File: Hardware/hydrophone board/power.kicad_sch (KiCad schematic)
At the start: 17 parts, among them J203 Screw_Terminal_01x02, U5 LT1963AxST-3.3

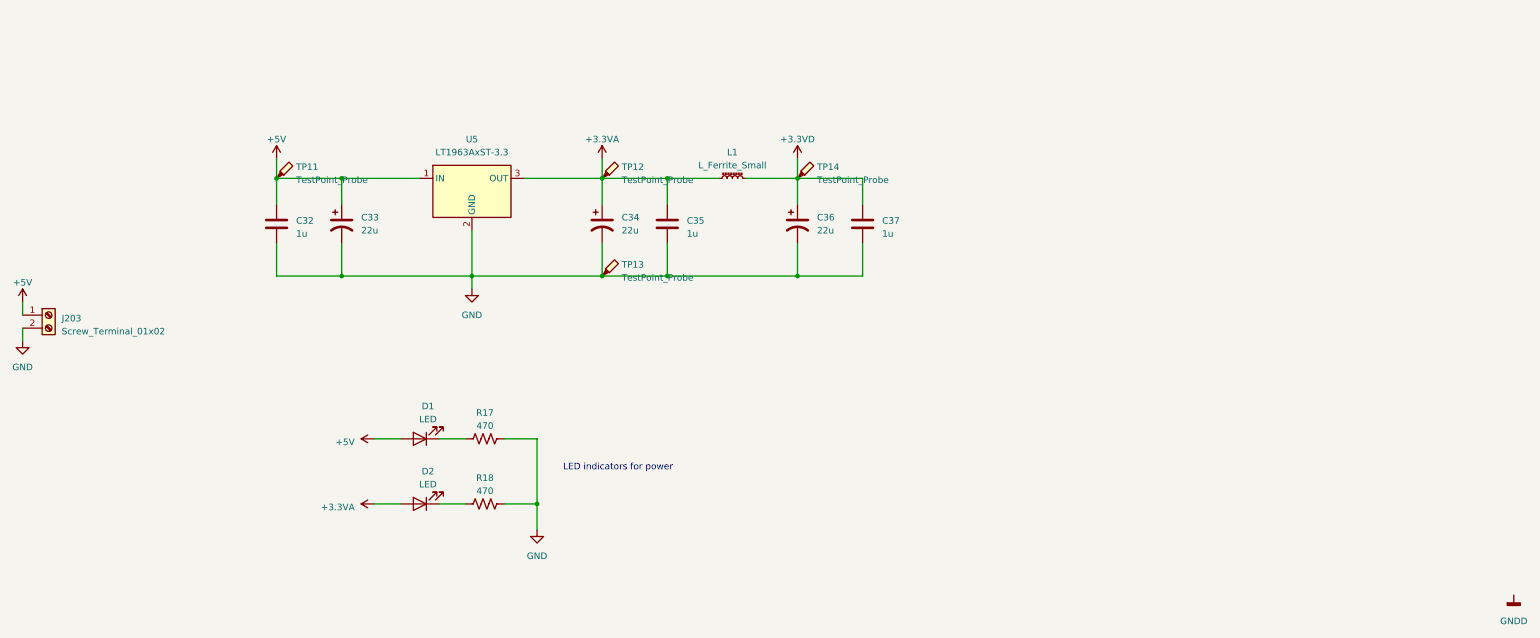
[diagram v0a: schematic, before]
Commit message: i2c pull ups
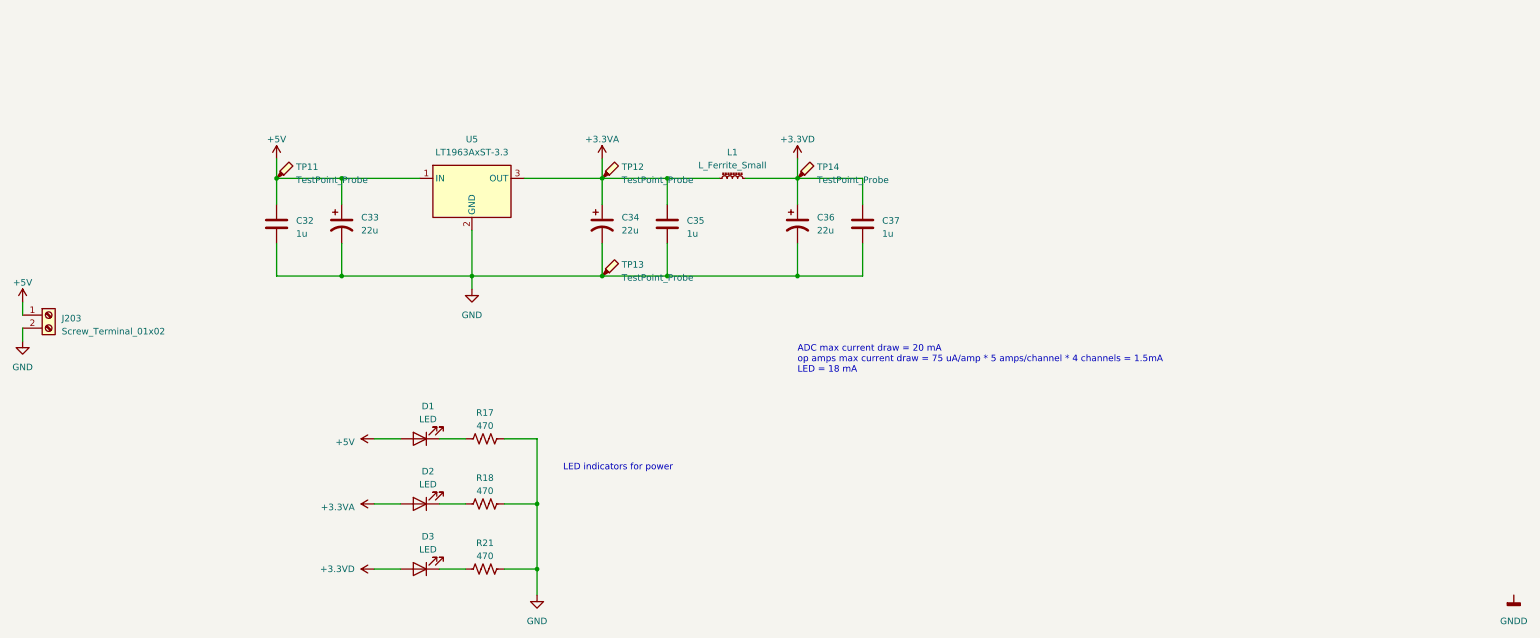
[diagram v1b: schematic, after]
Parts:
- added D3: LED, symbol Device:LED
- added R21: 470, symbol Device:R_US
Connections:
- net +3.3VD: now also D3.2 (A)
- net GND: now also R21.2
- new net: D3.1 (K), R21.1
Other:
- note added: "ADC max current draw = 20 mA op amps max current draw = 75 uA/amp * 5 amps/channel * 4 channels = 1.5mA LED = 18 mA"
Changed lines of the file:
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@@
   (junction (at 165.1 95.25) (diameter 0) (color 0 0 0 0)
   )
+  (junction (at 139.7 152.4) (diameter 0) (color 0 0 0 0)
+  )
   (junction (at 101.6 76.2) (diameter 0) (color 0 0 0 0)
   )
@@
     (stroke (width 0) (type default))
   )
-  (wire (pts (xy 139.7 139.7) (xy 139.7 144.78))
+  (wire (pts (xy 139.7 139.7) (xy 139.7 152.4))
     (stroke (width 0) (type default))
   )
@@
     (stroke (width 0) (type default))
   )
+  (wire (pts (xy 107.95 152.4) (xy 113.03 152.4))
+    (stroke (width 0) (type default))
+  )
   (wire (pts (xy 180.34 76.2) (xy 190.5 76.2))
     (stroke (width 0) (type default))
@@
     (stroke (width 0) (type default))
   )
+  (wire (pts (xy 120.65 152.4) (xy 125.73 152.4))
+    (stroke (width 0) (type default))
+  )
   (wire (pts (xy 107.95 127) (xy 113.03 127))
     (stroke (width 0) (type default))
   )
+  (wire (pts (xy 133.35 152.4) (xy 139.7 152.4))
+    (stroke (width 0) (type default))
+  )
   (wire (pts (xy 101.6 76.2) (xy 101.6 81.28))
     (stroke (width 0) (type default))
@@
     (stroke (width 0) (type default))
   )
+  (wire (pts (xy 139.7 152.4) (xy 139.7 157.48))
+    (stroke (width 0) (type default))
+  )
   (wire (pts (xy 165.1 76.2) (xy 165.1 81.28))
     (stroke (width 0) (type default))
+  )
+  (text "ADC max current draw = 20 mA\nop amps max current draw = 75 uA/amp * 5 amps/channel * 4 channels = 1.5mA\nLED = 18 mA"
+    (at 190.5 114.3 0)
+    (effects (font (size 1.27 1.27)) (justify left bottom))
   )
   (text "LED indicators for power" (at 144.78 133.35 0)
@@
     )
   )
+  (symbol (lib_id "power:+3.3V") (at 107.95 152.4 90) (unit 1)
+    (in_bom yes) (on_board yes) (dnp no) (fields_autoplaced)
+    (property "Reference" "#PWR?" (at 111.76 152.4 0)
+      (effects (font (size 1.27 1.27)) hide)
+    )
+    (property "Value" "+3.3VD" (at 104.14 152.4 90)
+      (effects (font (size 1.27 1.27)) (justify left))
+    )
+    (property "Footprint" "" (at 107.95 152.4 0)
+      (effects (font (size 1.27 1.27)) hide)
+    )
+    (property "Datasheet" "" (at 107.95 152.4 0)
+      (effects (font (size 1.27 1.27)) hide)
+    )
+    (pin "1")
+    (instances
+      (project "hydrophone board"
+        (path "/4356d3a6-6a00-447d-897e-473f60221539/c9760799-658d-4181-af96-8731ebbcaea9"
+          (reference "#PWR?") (unit 1)
+        )
+        (path "/4356d3a6-6a00-447d-897e-473f60221539/cf9d259f-9643-49eb-8aca-1ca8b75f4d64"
+          (reference "#PWR036") (unit 1)
+        )
+      )
+    )
+  )
   (symbol (lib_id "power:GND") (at 39.37 107.95 0) (unit 1)
     (in_bom yes) (on_board yes) (dnp no) (fields_autoplaced)
@@
     )
   )
+  (symbol (lib_id "Device:R_US") (at 129.54 152.4 90) (unit 1)
+    (in_bom yes) (on_board yes) (dnp no) (fields_autoplaced)
+    (property "Reference" "R21" (at 129.54 147.32 90)
+      (effects (font (size 1.27 1.27)))
+    )
+    (property "Value" "470" (at 129.54 149.86 90)
+      (effects (font (size 1.27 1.27)))
+    )
+    (property "Footprint" "" (at 129.794 151.384 90)
+      (effects (font (size 1.27 1.27)) hide)
+    )
+    (property "Datasheet" "~" (at 129.54 152.4 0)
+      (effects (font (size 1.27 1.27)) hide)
+    )
+    (pin "1")
+    (pin "2")
+    (instances
+      (project "hydrophone board"
+        (path "/4356d3a6-6a00-447d-897e-473f60221539/cf9d259f-9643-49eb-8aca-1ca8b75f4d64"
+          (reference "R21") (unit 1)
+        )
+      )
+    )
+  )
   (symbol (lib_id "Device:C_Polarized_US") (at 152.4 85.09 0) (unit 1)
     (in_bom yes) (on_board yes) (dnp no) (fields_autoplaced)
@@
         (path "/4356d3a6-6a00-447d-897e-473f60221539/cf9d259f-9643-49eb-8aca-1ca8b75f4d64"
           (reference "C34") (unit 1)
+        )
+      )
+    )
+  )
+  (symbol (lib_id "power:GND") (at 139.7 157.48 0) (unit 1)
+    (in_bom yes) (on_board yes) (dnp no) (fields_autoplaced)
+    (property "Reference" "#PWR0205" (at 139.7 163.83 0)
+      (effects (font (size 1.27 1.27)) hide)
+    )
+    (property "Value" "GND" (at 139.7 162.56 0)
+      (effects (font (size 1.27 1.27)))
+    )
+    (property "Footprint" "" (at 139.7 157.48 0)
+      (effects (font (size 1.27 1.27)) hide)
+    )
+    (property "Datasheet" "" (at 139.7 157.48 0)
+      (effects (font (size 1.27 1.27)) hide)
+    )
+    (pin "1")
+    (instances
+      (project "hydrophone board"
+        (path "/4356d3a6-6a00-447d-897e-473f60221539/1cfbaf71-7039-4355-8fc7-d8c77f0e8058"
+          (reference "#PWR0205") (unit 1)
+        )
+        (path "/4356d3a6-6a00-447d-897e-473f60221539/cf9d259f-9643-49eb-8aca-1ca8b75f4d64"
+          (reference "#PWR045") (unit 1)
         )
       )
@@
     )
   )
-  (symbol (lib_id "power:GND") (at 139.7 144.78 0) (unit 1)
-    (in_bom yes) (on_board yes) (dnp no) (fields_autoplaced)
-    (property "Reference" "#PWR0205" (at 139.7 151.13 0)
-      (effects (font (size 1.27 1.27)) hide)
-    )
-    (property "Value" "GND" (at 139.7 149.86 0)
-      (effects (font (size 1.27 1.27)))
-    )
-    (property "Footprint" "" (at 139.7 144.78 0)
-      (effects (font (size 1.27 1.27)) hide)
-    )
-    (property "Datasheet" "" (at 139.7 144.78 0)
-      (effects (font (size 1.27 1.27)) hide)
-    )
-    (pin "1")
-    (instances
-      (project "hydrophone board"
-        (path "/4356d3a6-6a00-447d-897e-473f60221539/1cfbaf71-7039-4355-8fc7-d8c77f0e8058"
-          (reference "#PWR0205") (unit 1)
-        )
-        (path "/4356d3a6-6a00-447d-897e-473f60221539/cf9d259f-9643-49eb-8aca-1ca8b75f4d64"
-          (reference "#PWR036") (unit 1)
-        )
-      )
-    )
-  )
   (symbol (lib_id "Device:LED") (at 116.84 127 180) (unit 1)
     (in_bom yes) (on_board yes) (dnp no) (fields_autoplaced)
@@
         )
       )
+    )
+  )
+  (symbol (lib_id "Device:LED") (at 116.84 152.4 180) (unit 1)
+    (in_bom yes) (on_board yes) (dnp no) (fields_autoplaced)
+    (property "Reference" "D3" (at 118.4275 146.05 0)
+      (effects (font (size 1.27 1.27)))
+    )
+    (property "Value" "LED" (at 118.4275 148.59 0)
+      (effects (font (size 1.27 1.27)))
+    )
+    (property "Footprint" "" (at 116.84 152.4 0)
+      (effects (font (size 1.27 1.27)) hide)
+    )
+    (property "Datasheet" "~" (at 116.84 152.4 0)
+      (effects (font (size 1.27 1.27)) hide)
+    )
+    (pin "1")
+    (pin "2")
+    (instances
+      (project "hydrophone board"
+        (path "/4356d3a6-6a00-447d-897e-473f60221539/cf9d259f-9643-49eb-8aca-1ca8b75f4d64"
+          (reference "D3") (unit 1)
+        )
+      )

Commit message: changed connectors
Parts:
- removed D3: LED, symbol Device:LED
- removed J203: Screw_Terminal_01x02, symbol Connector:Screw_Terminal_01x02
- removed R21: 470, symbol Device:R_US
- added J8: Conn_01x03, symbol Connector_Generic:Conn_01x03
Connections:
- net +3.3VA: now also J8.2 (Pin_2); no longer U5.3 (OUT)
- new net: J8.1 (Pin_1), U5.3 (OUT)
- new net 3.3V MCU: J8.3 (Pin_3)

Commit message: removed some connectors
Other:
- note added: "choose 3.3V from MCU or linear regulator"
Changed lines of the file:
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@@
     (stroke (width 0) (type default))
+  )
+  (text "choose 3.3V from MCU or linear regulator" (at 133.35 45.72 0)
+    (effects (font (size 1.27 1.27)) (justify left bottom))
   )
   (text "ADC max current draw = 20 mA\nop amps max current draw = 75 uA/amp * 5 amps/channel * 4 channels = 1.5mA\nLED = 18 mA"

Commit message: annotate all component
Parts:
- renumbered C32 to C401, C33 to C402, C34 to C403, C35 to C404, C36 to C405, C37 to C406, D1 to D401, D2 to D402, J8 to J401, L1 to L401, R17 to R401, R18 to R402, TP11 to TP401, TP12 to TP402, TP14 to TP403, TP13 to TP404, U5 to U401

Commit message: assigned footprints
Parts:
- C501: renamed from C401; footprint (none) -> Capacitor_SMD:C_0603_1608Metric
- C502: renamed from C402; footprint (none) -> Capacitor_SMD:C_0805_2012Metric
- C503: renamed from C403; footprint (none) -> Capacitor_SMD:C_0805_2012Metric
- C504: renamed from C404; footprint (none) -> Capacitor_SMD:C_0603_1608Metric
- C505: renamed from C405; footprint (none) -> Capacitor_SMD:C_0805_2012Metric
- C506: renamed from C406; footprint (none) -> Capacitor_SMD:C_0603_1608Metric
- D501: renamed from D401; footprint (none) -> LED_SMD:LED_0805_2012Metric
- D502: renamed from D402; footprint (none) -> LED_SMD:LED_0805_2012Metric
- J501: renamed from J401; footprint (none) -> Connector_PinSocket_2.54mm:PinSocket_1x03_P2.54mm_Vertical
- L501: renamed from L401; footprint (none) -> Inductor_SMD:L_0805_2012Metric
- R501: renamed from R401; footprint (none) -> Resistor_SMD:R_0603_1608Metric
- R502: renamed from R402; footprint (none) -> Resistor_SMD:R_0603_1608Metric
- TP501: renamed from TP401; footprint (none) -> Connector_PinHeader_2.54mm:PinHeader_1x01_P2.54mm_Vertical
- TP502: renamed from TP402; footprint (none) -> Connector_PinHeader_2.54mm:PinHeader_1x01_P2.54mm_Vertical
- TP503: renamed from TP403; footprint (none) -> Connector_PinHeader_2.54mm:PinHeader_1x01_P2.54mm_Vertical
- TP504: renamed from TP404; footprint (none) -> Connector_PinHeader_2.54mm:PinHeader_1x01_P2.54mm_Vertical
- renumbered U401 to U501

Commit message: resolved ERC errors and changed mic bias resistor for 3.3V
1.1k -> 360 ohm
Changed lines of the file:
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@@
   (junction (at 190.5 76.2) (diameter 0) (color 0 0 0 0)
   )
+  (junction (at 203.2 76.2) (diameter 0) (color 0 0 0 0)
+  )
   (junction (at 165.1 95.25) (diameter 0) (color 0 0 0 0)
   )
@@
   (junction (at 88.9 76.2) (diameter 0) (color 0 0 0 0)
   )
+  (junction (at 143.51 76.2) (diameter 0) (color 0 0 0 0)
+  )
+  (junction (at 88.9 95.25) (diameter 0) (color 0 0 0 0)
+  )
   (junction (at 190.5 95.25) (diameter 0) (color 0 0 0 0)
   )
@@
   )
   (wire (pts (xy 101.6 95.25) (xy 101.6 88.9))
+    (stroke (width 0) (type default))
+  )
+  (wire (pts (xy 203.2 73.66) (xy 203.2 76.2))
     (stroke (width 0) (type default))
   )
@@
     )
   )
+  (symbol (lib_id "PCM_4ms_Power-symbol:PWR_FLAG") (at 203.2 73.66 0) (unit 1)
+    (in_bom yes) (on_board yes) (dnp no) (fields_autoplaced)
+    (property "Reference" "#FLG0244" (at 203.2 71.755 0)
+      (effects (font (size 1.27 1.27)) hide)
+    )
+    (property "Value" "PWR_FLAG" (at 203.2 68.58 0)
+      (effects (font (size 1.27 1.27)))
+    )
+    (property "Footprint" "" (at 203.2 73.66 0)
+      (effects (font (size 1.27 1.27)) hide)
+    )
+    (property "Datasheet" "" (at 203.2 73.66 0)
+      (effects (font (size 1.27 1.27)) hide)
+    )
+    (pin "1")
+    (instances
+      (project "hydrophone board"
+        (path "/4356d3a6-6a00-447d-897e-473f60221539/cf9d259f-9643-49eb-8aca-1ca8b75f4d64"
+          (reference "#FLG0244") (unit 1)
+        )
+      )
+    )
+  )
   (symbol (lib_id "power:+3.3VA") (at 107.95 139.7 90) (unit 1)
     (in_bom yes) (on_board yes) (dnp no) (fields_autoplaced)
@@
         (path "/4356d3a6-6a00-447d-897e-473f60221539/cf9d259f-9643-49eb-8aca-1ca8b75f4d64"
           (reference "TP503") (unit 1)
-        )
-      )
-    )
-  )
-  (symbol (lib_id "power:GNDD") (at 330.2 157.48 0) (unit 1)
-    (in_bom yes) (on_board yes) (dnp no) (fields_autoplaced)
-    (property "Reference" "#PWR?" (at 330.2 163.83 0)
-      (effects (font (size 1.27 1.27)) hide)
-    )
-    (property "Value" "GNDD" (at 330.2 162.56 0)
-      (effects (font (size 1.27 1.27)))
-    )
-    (property "Footprint" "" (at 330.2 157.48 0)
-      (effects (font (size 1.27 1.27)) hide)
-    )
-    (property "Datasheet" "" (at 330.2 157.48 0)
-      (effects (font (size 1.27 1.27)) hide)
-    )
-    (pin "1")
-    (instances
-      (project "hydrophone board"
-        (path "/4356d3a6-6a00-447d-897e-473f60221539/c9760799-658d-4181-af96-8731ebbcaea9"
-          (reference "#PWR?") (unit 1)
-        )
-        (path "/4356d3a6-6a00-447d-897e-473f60221539/cf9d259f-9643-49eb-8aca-1ca8b75f4d64"
-          (reference "#PWR0508") (unit 1)
         )
       )
@@
     )
   )
+  (symbol (lib_id "PCM_4ms_Power-symbol:PWR_FLAG") (at 143.51 76.2 180) (unit 1)
+    (in_bom yes) (on_board yes) (dnp no) (fields_autoplaced)
+    (property "Reference" "#FLG0243" (at 143.51 78.105 0)
+      (effects (font (size 1.27 1.27)) hide)
+    )
+    (property "Value" "PWR_FLAG" (at 143.51 81.28 0)
+      (effects (font (size 1.27 1.27)))
+    )
+    (property "Footprint" "" (at 143.51 76.2 0)
+      (effects (font (size 1.27 1.27)) hide)
+    )
+    (property "Datasheet" "" (at 143.51 76.2 0)
+      (effects (font (size 1.27 1.27)) hide)
+    )
+    (pin "1")
+    (instances
+      (project "hydrophone board"
+        (path "/4356d3a6-6a00-447d-897e-473f60221539/cf9d259f-9643-49eb-8aca-1ca8b75f4d64"
+          (reference "#FLG0243") (unit 1)
+        )
+      )
+    )
+  )
   (symbol (lib_id "Device:C") (at 165.1 85.09 0) (unit 1)
     (in_bom yes) (on_board yes) (dnp no) (fields_autoplaced)
@@
         )
       )
+    )
+  )
+  (symbol (lib_id "power:PWR_FLAG") (at 88.9 76.2 90) (unit 1)
+    (in_bom yes) (on_board yes) (dnp no) (fields_autoplaced)
+    (property "Reference" "#FLG0241" (at 86.995 76.2 0)
+      (effects (font (size 1.27 1.27)) hide)
+    )
+    (property "Value" "PWR_FLAG" (at 85.09 76.2 90)
+      (effects (font (size 1.27 1.27)) (justify left))
+    )
+    (property "Footprint" "" (at 88.9 76.2 0)
+      (effects (font (size 1.27 1.27)) hide)
+    )
+    (property "Datasheet" "~" (at 88.9 76.2 0)
+      (effects (font (size 1.27 1.27)) hide)
+    )
+    (pin "1")
+    (instances
+      (project "hydrophone board"
+        (path "/4356d3a6-6a00-447d-897e-473f60221539/cf9d259f-9643-49eb-8aca-1ca8b75f4d64"
+          (reference "#FLG0241") (unit 1)
+        )
+      )
+    )
+  )
+  (symbol (lib_id "power:PWR_FLAG") (at 88.9 95.25 90) (unit 1)
+    (in_bom yes) (on_board yes) (dnp no) (fields_autoplaced)
+    (property "Reference" "#FLG0242" (at 86.995 95.25 0)
+      (effects (font (size 1.27 1.27)) hide)
+    )
+    (property "Value" "PWR_FLAG" (at 85.09 95.25 90)
+      (effects (font (size 1.27 1.27)) (justify left))
+    )
+    (property "Footprint" "" (at 88.9 95.25 0)
+      (effects (font (size 1.27 1.27)) hide)
+    )
+    (property "Datasheet" "~" (at 88.9 95.25 0)
+      (effects (font (size 1.27 1.27)) hide)
+    )
+    (pin "1")
+    (instances
+      (project "hydrophone board"
+        (path "/4356d3a6-6a00-447d-897e-473f60221539/cf9d259f-9643-49eb-8aca-1ca8b75f4d64"
+          (reference "#FLG0242") (unit 1)
+        )
+      )

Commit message: changed all cap + resistors to 0805, starting filter layout
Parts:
- C501, C504, C506: footprint Capacitor_SMD:C_0603_1608Metric -> Capacitor_SMD:C_0805_2012Metric_Pad1.18x1.45mm_HandSolder
- C502, C503, C505: footprint Capacitor_SMD:C_0805_2012Metric -> Capacitor_SMD:C_0805_2012Metric_Pad1.18x1.45mm_HandSolder
- D501, D502: footprint LED_SMD:LED_0805_2012Metric -> LED_SMD:LED_1206_3216Metric_Pad1.42x1.75mm_HandSolder
- L501: footprint Inductor_SMD:L_0805_2012Metric -> Inductor_SMD:L_0805_2012Metric_Pad1.05x1.20mm_HandSolder
- R501, R502: footprint Resistor_SMD:R_0603_1608Metric -> Resistor_SMD:R_0805_2012Metric_Pad1.20x1.40mm_HandSolder
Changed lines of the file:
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@@
       (effects (font (size 1.27 1.27)))
     )
-    (property "Footprint" "Inductor_SMD:L_0805_2012Metric" (at 177.8 76.2 0)
+    (property "Footprint" "Inductor_SMD:L_0805_2012Metric_Pad1.05x1.20mm_HandSolder" (at 177.8 76.2 0)
       (effects (font (size 1.27 1.27)) hide)
     )
@@
       (effects (font (size 1.27 1.27)) (justify left))
     )
-    (property "Footprint" "Capacitor_SMD:C_0805_2012Metric" (at 101.6 85.09 0)
+    (property "Footprint" "Capacitor_SMD:C_0805_2012Metric_Pad1.18x1.45mm_HandSolder" (at 101.6 85.09 0)
       (effects (font (size 1.27 1.27)) hide)
     )
@@
       (effects (font (size 1.27 1.27)))
     )
-    (property "Footprint" "LED_SMD:LED_0805_2012Metric" (at 116.84 139.7 0)
+    (property "Footprint" "LED_SMD:LED_1206_3216Metric_Pad1.42x1.75mm_HandSolder" (at 116.84 139.7 0)
       (effects (font (size 1.27 1.27)) hide)
     )
@@
       (effects (font (size 1.27 1.27)) (justify left))
     )
-    (property "Footprint" "Capacitor_SMD:C_0603_1608Metric" (at 89.8652 88.9 0)
+    (property "Footprint" "Capacitor_SMD:C_0805_2012Metric_Pad1.18x1.45mm_HandSolder" (at 89.8652 88.9 0)
       (effects (font (size 1.27 1.27)) hide)
     )
@@
       (effects (font (size 1.27 1.27)) (justify left))
     )
-    (property "Footprint" "Capacitor_SMD:C_0603_1608Metric" (at 204.1652 88.9 0)
+    (property "Footprint" "Capacitor_SMD:C_0805_2012Metric_Pad1.18x1.45mm_HandSolder" (at 204.1652 88.9 0)
       (effects (font (size 1.27 1.27)) hide)
     )
@@
       (effects (font (size 1.27 1.27)) (justify left))
     )
-    (property "Footprint" "Capacitor_SMD:C_0805_2012Metric" (at 152.4 85.09 0)
+    (property "Footprint" "Capacitor_SMD:C_0805_2012Metric_Pad1.18x1.45mm_HandSolder" (at 152.4 85.09 0)
       (effects (font (size 1.27 1.27)) hide)
     )
@@
       (effects (font (size 1.27 1.27)))
     )
-    (property "Footprint" "Resistor_SMD:R_0603_1608Metric" (at 129.794 138.684 90)
+    (property "Footprint" "Resistor_SMD:R_0805_2012Metric_Pad1.20x1.40mm_HandSolder" (at 129.794 138.684 90)
       (effects (font (size 1.27 1.27)) hide)
     )
@@
       (effects (font (size 1.27 1.27)) (justify left))
     )
-    (property "Footprint" "Capacitor_SMD:C_0603_1608Metric" (at 166.0652 88.9 0)
+    (property "Footprint" "Capacitor_SMD:C_0805_2012Metric_Pad1.18x1.45mm_HandSolder" (at 166.0652 88.9 0)
       (effects (font (size 1.27 1.27)) hide)
     )
@@
       (effects (font (size 1.27 1.27)))
     )
-    (property "Footprint" "LED_SMD:LED_0805_2012Metric" (at 116.84 127 0)
+    (property "Footprint" "LED_SMD:LED_1206_3216Metric_Pad1.42x1.75mm_HandSolder" (at 116.84 127 0)
       (effects (font (size 1.27 1.27)) hide)
     )
@@
       (effects (font (size 1.27 1.27)))
     )
-    (property "Footprint" "Resistor_SMD:R_0603_1608Metric" (at 129.794 125.984 90)
+    (property "Footprint" "Resistor_SMD:R_0805_2012Metric_Pad1.20x1.40mm_HandSolder" (at 129.794 125.984 90)
       (effects (font (size 1.27 1.27)) hide)
     )
@@
       (effects (font (size 1.27 1.27)) (justify left))
     )
-    (property "Footprint" "Capacitor_SMD:C_0805_2012Metric" (at 190.5 85.09 0)
-      (effects (font (size 1.27 1.27)) hide)
-    )
+    (property "Footprint" "Capacitor_SMD:C_0805_2012Metric_Pad1.18x1.45mm_HandSolder" (at 190.5 85.09 0)
+      (effects (font (size 1.27 1.27)) hide)
+    )
